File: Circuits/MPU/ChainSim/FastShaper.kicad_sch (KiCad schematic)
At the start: 34 parts, among them U3 ADA4805-2ARMZ, U4 ADA4805-2ARMZ

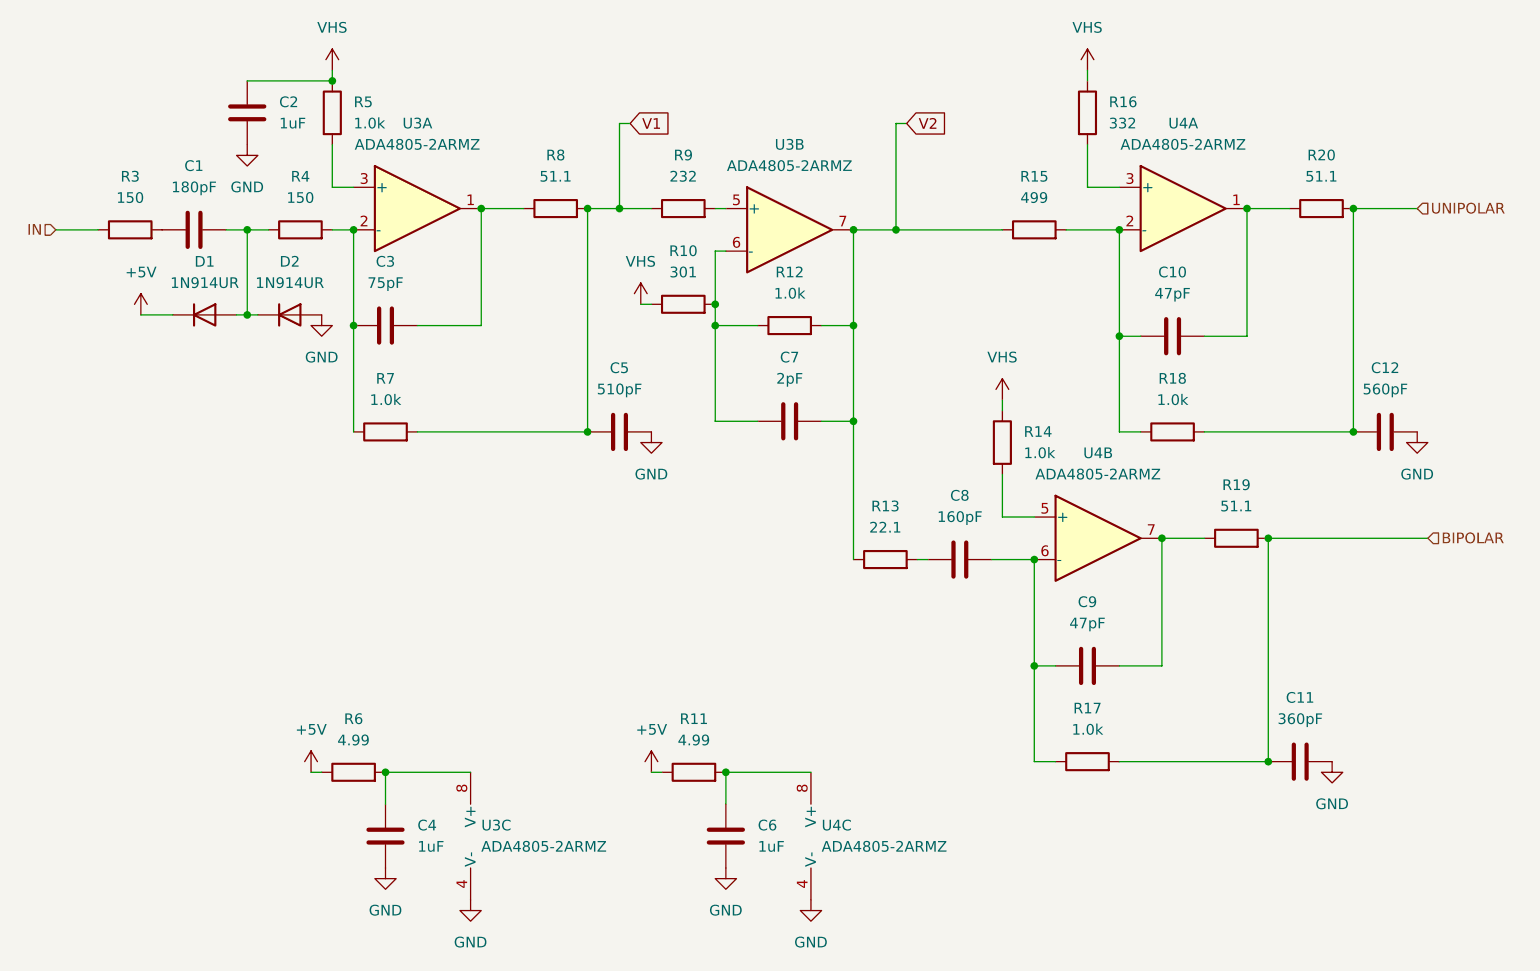
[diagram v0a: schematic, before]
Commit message: Chainsim working, a little tuneup
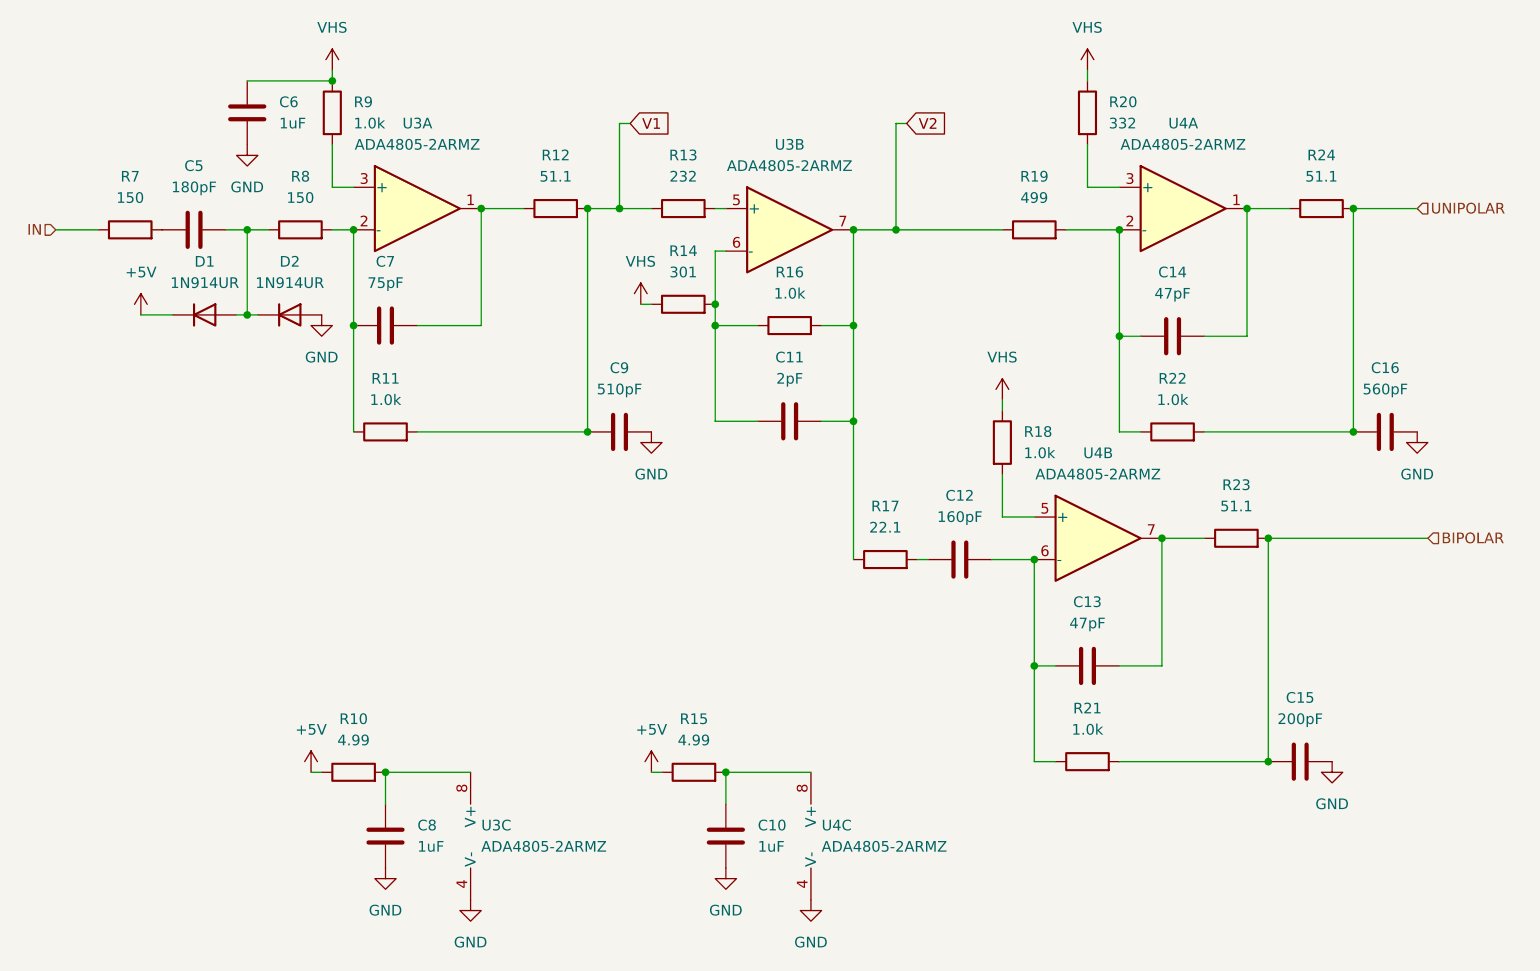
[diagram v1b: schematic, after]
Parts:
- C15: renamed from C11; value 360pF -> 200pF
- renumbered C6 to C10, C7 to C11, C8 to C12, C9 to C13, C10 to C14, C12 to C16, C1 to C5, C2 to C6, C3 to C7, C4 to C8, C5 to C9, R6 to R10, R7 to R11, R8 to R12, R9 to R13, R10 to R14, R11 to R15, R12 to R16, R13 to R17, R14 to R18, R15 to R19, R16 to R20, R17 to R21, R18 to R22, R19 to R23, R20 to R24, R3 to R7, R4 to R8, R5 to R9
